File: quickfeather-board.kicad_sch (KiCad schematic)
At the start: 101 parts, among them IC1 EOSAI-S-PUN64, J1 PinHeader_1x2_P2.54mm_Drill1.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, J2 PinHeader_1x12_P2.54m_Drill1.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, J3 61301611121, J4 S2B-PH-SM4-TB(LF)(SN), J5 USB-Micro-B_Molex_473460001, J6 PinHeader_2x5_P1.27mm_SMD_Lat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, J7 PinHeader_1x2_P2.54mm_Drill1.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, J8 PinHeader_2x8_P2.54mm_Drill1mm, M1 mounting_pad, M2 mounting_pad, M3 mounting_pad, M4 mounting_pad, Q1 NX3008CBKV, Q2 2N7002PV, Q3 2N7002PV, Q4 DMG1012T-7, U1 TPS62821DLCR, U2 MCP73831T-2AC_SOT, U3 GD25Q16CWIGR, U4 DPS310, U5 MC3635, X1 Resonator_12MHz_445

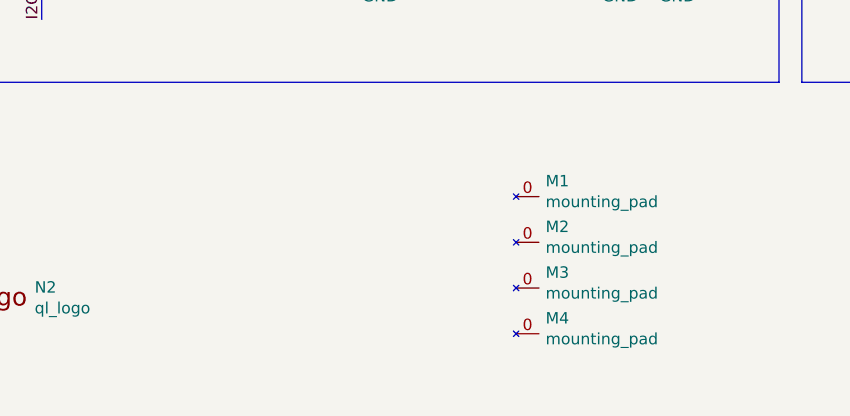
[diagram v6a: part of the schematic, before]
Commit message: [#54927] Add mounting holes
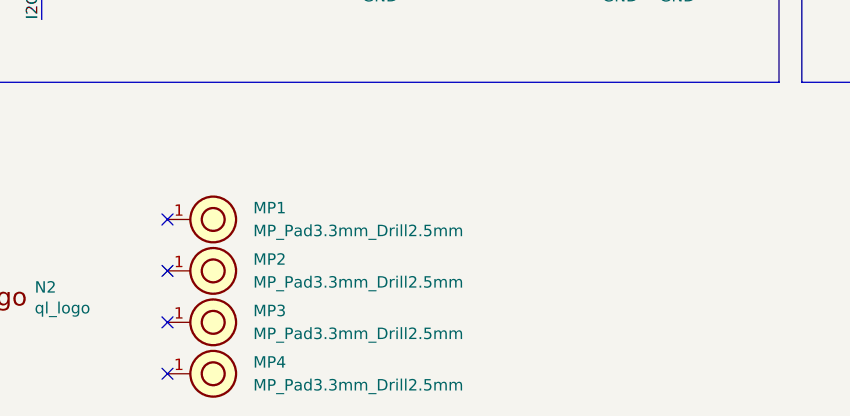
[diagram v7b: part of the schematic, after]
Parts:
- removed M1, M2, M3, M4: mounting_pad, quicklogic-quickfeather-board-footprints:mpad, symbol quickfeather-board:mounting_pad
- added MP1, MP2, MP3, MP4: MP_Pad3.3mm_Drill2.5mm, antmicro-footprints:MP_Pad3.3mm_Drill2.5mm, symbol antmicroMechanicalParts:MP_Pad3.3mm_Drill2.5mm
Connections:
- no-connect marks 23 -> 27
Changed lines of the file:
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@@
   (no_connect (at 344.17 41.91))
   (no_connect (at 389.89 159.385))
+  (no_connect (at 238.125 280.035))
   (no_connect (at 389.255 200.66))
   (no_connect (at 287.02 116.205))
@@
   (no_connect (at 375.92 61.595))
   (no_connect (at 354.33 39.37))
+  (no_connect (at 238.125 268.605))
   (no_connect (at 240.03 95.25))
   (no_connect (at 297.18 116.205))
+  (no_connect (at 238.125 274.32))
   (no_connect (at 27.305 219.075))
   (no_connect (at 297.18 128.905))
   (no_connect (at 359.41 102.87))
+  (no_connect (at 238.125 262.89))
   (no_connect (at 342.9 228.6))
   (no_connect (at 27.305 216.535))
@@
     )
   )
-  (symbol (lib_id "quickfeather-board:mounting_pad") (at 276.86 260.35 0) (unit 1)
-    (in_bom yes) (on_board yes) (dnp no)
-    (property "Reference" "M1" (at 280.1366 258.6228 0)
-      (effects (font (size 1.27 1.27)) (justify left))
-    )
-    (property "Value" "mounting_pad" (at 280.1366 260.9342 0)
-      (effects (font (size 1.27 1.27)) (justify left))
-    )
-    (property "Footprint" "quicklogic-quickfeather-board-footprints:mpad" (at 284.48 263.525 0)
-      (effects (font (size 1.27 1.27)) hide)
-    )
-    (property "Datasheet" "" (at 276.86 260.35 0)
-      (effects (font (size 1.27 1.27)) hide)
-    )
-    (pin "0")
-    (instances
-      (project "quickfeather-board"
-        (path "/902b299f-3bfc-46c5-8ba2-656b16e1e538"
-          (reference "M1") (unit 1)
-        )
-      )
-    )
-  )
-  (symbol (lib_id "quickfeather-board:mounting_pad") (at 276.86 265.43 0) (unit 1)
-    (in_bom yes) (on_board yes) (dnp no)
-    (property "Reference" "M2" (at 280.1366 263.7028 0)
-      (effects (font (size 1.27 1.27)) (justify left))
-    )
-    (property "Value" "mounting_pad" (at 280.1366 266.0142 0)
-      (effects (font (size 1.27 1.27)) (justify left))
-    )
-    (property "Footprint" "quicklogic-quickfeather-board-footprints:mpad" (at 284.48 268.605 0)
-      (effects (font (size 1.27 1.27)) hide)
-    )
-    (property "Datasheet" "" (at 276.86 265.43 0)
-      (effects (font (size 1.27 1.27)) hide)
-    )
-    (pin "0")
-    (instances
-      (project "quickfeather-board"
-        (path "/902b299f-3bfc-46c5-8ba2-656b16e1e538"
-          (reference "M2") (unit 1)
-        )
-      )
-    )
-  )
-  (symbol (lib_id "quickfeather-board:mounting_pad") (at 276.86 270.51 0) (unit 1)
-    (in_bom yes) (on_board yes) (dnp no)
-    (property "Reference" "M3" (at 280.1366 268.7828 0)
-      (effects (font (size 1.27 1.27)) (justify left))
-    )
-    (property "Value" "mounting_pad" (at 280.1366 271.0942 0)
-      (effects (font (size 1.27 1.27)) (justify left))
-    )
-    (property "Footprint" "quicklogic-quickfeather-board-footprints:mpad" (at 284.48 273.685 0)
-      (effects (font (size 1.27 1.27)) hide)
-    )
-    (property "Datasheet" "" (at 276.86 270.51 0)
-      (effects (font (size 1.27 1.27)) hide)
-    )
-    (pin "0")
-    (instances
-      (project "quickfeather-board"
-        (path "/902b299f-3bfc-46c5-8ba2-656b16e1e538"
-          (reference "M3") (unit 1)
-        )
-      )
-    )
-  )
-  (symbol (lib_id "quickfeather-board:mounting_pad") (at 276.86 275.59 0) (unit 1)
-    (in_bom yes) (on_board yes) (dnp no)
-    (property "Reference" "M4" (at 280.1366 273.8628 0)
-      (effects (font (size 1.27 1.27)) (justify left))
-    )
-    (property "Value" "mounting_pad" (at 280.1366 276.1742 0)
-      (effects (font (size 1.27 1.27)) (justify left))
-    )
-    (property "Footprint" "quicklogic-quickfeather-board-footprints:mpad" (at 284.48 278.765 0)
-      (effects (font (size 1.27 1.27)) hide)
-    )
-    (property "Datasheet" "" (at 276.86 275.59 0)
-      (effects (font (size 1.27 1.27)) hide)
-    )
-    (pin "0")
-    (instances
-      (project "quickfeather-board"
-        (path "/902b299f-3bfc-46c5-8ba2-656b16e1e538"
-          (reference "M4") (unit 1)
-        )
-      )
-    )
-  )
   (symbol (lib_id "antmicropower:+3V3") (at 375.285 24.13 0) (unit 1)
     (in_bom yes) (on_board yes) (dnp no)
@@
     )
   )
+  (symbol (lib_id "antmicroMechanicalParts:MP_Pad3.3mm_Drill2.5mm") (at 238.125 280.035 0) (unit 1)
+    (in_bom no) (on_board yes) (dnp no) (fields_autoplaced)
+    (property "Reference" "MP4" (at 247.65 278.765 0)
+      (effects (font (size 1.27 1.27) (thickness 0.15)) (justify left))
+    )
+    (property "Value" "MP_Pad3.3mm_Drill2.5mm" (at 247.65 281.305 0)
+      (effects (font (size 1.27 1.27) (thickness 0.15)) (justify left))
+    )
+    (property "Footprint" "antmicro-footprints:MP_Pad3.3mm_Drill2.5mm" (at 250.825 286.385 0)
+      (effects (font (size 1.27 1.27) (thickness 0.15)) (justify left bottom) hide)
+    )
+    (property "Datasheet" "" (at 254.965 295.605 0)
+      (effects (font (size 1.27 1.27) (thickness 0.15)) (justify left bottom) hide)
+    )
+    (property "License" "Apache-2.0" (at 250.825 291.465 0)
+      (effects (font (size 1.27 1.27)) (justify left bottom) hide)
+    )
+    (property "Author" " Antmicro" (at 249.555 288.925 0)
+      (effects (font (size 1.27 1.27)) (justify left bottom) hide)
+    )
+    (pin "1")
+    (instances
+      (project "quickfeather-board"
+        (path "/902b299f-3bfc-46c5-8ba2-656b16e1e538"
+          (reference "MP4") (unit 1)
+        )
+      )
+    )
+  )
   (symbol (lib_id "antmicropower:+3V3") (at 384.81 24.13 0) (unit 1)
     (in_bom yes) (on_board yes) (dnp no)
@@
     )
   )
+  (symbol (lib_id "antmicroMechanicalParts:MP_Pad3.3mm_Drill2.5mm") (at 238.125 274.32 0) (unit 1)
+    (in_bom no) (on_board yes) (dnp no) (fields_autoplaced)
+    (property "Reference" "MP3" (at 247.65 273.05 0)
+      (effects (font (size 1.27 1.27) (thickness 0.15)) (justify left))
+    )
+    (property "Value" "MP_Pad3.3mm_Drill2.5mm" (at 247.65 275.59 0)
+      (effects (font (size 1.27 1.27) (thickness 0.15)) (justify left))
+    )
+    (property "Footprint" "antmicro-footprints:MP_Pad3.3mm_Drill2.5mm" (at 250.825 280.67 0)
+      (effects (font (size 1.27 1.27) (thickness 0.15)) (justify left bottom) hide)
+    )
+    (property "Datasheet" "" (at 254.965 289.89 0)
+      (effects (font (size 1.27 1.27) (thickness 0.15)) (justify left bottom) hide)
+    )
+    (property "License" "Apache-2.0" (at 250.825 285.75 0)
+      (effects (font (size 1.27 1.27)) (justify left bottom) hide)
+    )
+    (property "Author" " Antmicro" (at 249.555 283.21 0)
+      (effects (font (size 1.27 1.27)) (justify left bottom) hide)
+    )
+    (pin "1")
+    (instances
+      (project "quickfeather-board"
+        (path "/902b299f-3bfc-46c5-8ba2-656b16e1e538"
+          (reference "MP3") (unit 1)
+        )
+      )
+    )
+  )
   (symbol (lib_id "antmicropower:+3V3") (at 366.395 24.13 0) (unit 1)
     (in_bom yes) (on_board yes) (dnp no)
@@
     )
   )
+  (symbol (lib_id "antmicroMechanicalParts:MP_Pad3.3mm_Drill2.5mm") (at 238.125 262.89 0) (unit 1)
+    (in_bom no) (on_board yes) (dnp no) (fields_autoplaced)
+    (property "Reference" "MP1" (at 247.65 261.62 0)
+      (effects (font (size 1.27 1.27) (thickness 0.15)) (justify left))
+    )
+    (property "Value" "MP_Pad3.3mm_Drill2.5mm" (at 247.65 264.16 0)
+      (effects (font (size 1.27 1.27) (thickness 0.15)) (justify left))
+    )
+    (property "Footprint" "antmicro-footprints:MP_Pad3.3mm_Drill2.5mm" (at 250.825 269.24 0)
+      (effects (font (size 1.27 1.27) (thickness 0.15)) (justify left bottom) hide)
+    )
+    (property "Datasheet" "" (at 254.965 278.46 0)
+      (effects (font (size 1.27 1.27) (thickness 0.15)) (justify left bottom) hide)
+    )
+    (property "License" "Apache-2.0" (at 250.825 274.32 0)
+      (effects (font (size 1.27 1.27)) (justify left bottom) hide)
+    )
+    (property "Author" " Antmicro" (at 249.555 271.78 0)
+      (effects (font (size 1.27 1.27)) (justify left bottom) hide)
+    )
+    (pin "1")
+    (instances
+      (project "quickfeather-board"
+        (path "/902b299f-3bfc-46c5-8ba2-656b16e1e538"
+          (reference "MP1") (unit 1)
+        )
+      )
+    )
+  )
   (symbol (lib_id "antmicroCapacitors0603:C_4u7_0603") (at 262.89 177.165 270) (unit 1)
     (in_bom yes) (on_board yes) (dnp no) (fields_autoplaced)
@@
         )
       )
+    )
+  )
+  (symbol (lib_id "antmicroMechanicalParts:MP_Pad3.3mm_Drill2.5mm") (at 238.125 268.605 0) (unit 1)
+    (in_bom no) (on_board yes) (dnp no) (fields_autoplaced)
+    (property "Reference" "MP2" (at 247.65 267.335 0)
+      (effects (font (size 1.27 1.27) (thickness 0.15)) (justify left))
+    )
+    (property "Value" "MP_Pad3.3mm_Drill2.5mm" (at 247.65 269.875 0)
+      (effects (font (size 1.27 1.27) (thickness 0.15)) (justify left))
+    )
+    (property "Footprint" "antmicro-footprints:MP_Pad3.3mm_Drill2.5mm" (at 250.825 274.955 0)
+      (effects (font (size 1.27 1.27) (thickness 0.15)) (justify left bottom) hide)
+    )
+    (property "Datasheet" "" (at 254.965 284.175 0)
+      (effects (font (size 1.27 1.27) (thickness 0.15)) (justify left bottom) hide)
+    )
+    (property "License" "Apache-2.0" (at 250.825 280.035 0)
+      (effects (font (size 1.27 1.27)) (justify left bottom) hide)
+    )
+    (property "Author" " Antmicro" (at 249.555 277.495 0)
+      (effects (font (size 1.27 1.27)) (justify left bottom) hide)
+    )
+    (pin "1")
+    (instances
+      (project "quickfeather-board"
+        (path "/902b299f-3bfc-46c5-8ba2-656b16e1e538"
+          (reference "MP2") (unit 1)
+        )
+      )

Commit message: [#54927] Update X1
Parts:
- X1: value Resonator_12MHz_445 -> Resonator_32.768kHz_ECX-31B; footprint antmicro-footprints:Resonator_SMD_CTS_445_5x3.2mm -> antmicro-footprints:SMD-2_3.2x1.5mm; symbol antmicroResonators:Resonator_12MHz_445 -> antmicroResonators:Resonator_32.768kHz_ECX-31B; MPN 445I23D12M00000 -> ECS-.327-12.5-34B-TR; Manufacturer CTS -> ECS Inc. International; Val 12MHz -> 32.768 kHz
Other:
- moved on the sheet: C6, C7, X1
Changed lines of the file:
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@@
   (junction (at 356.87 130.81) (diameter 0) (color 0 0 0 0)
   )
+  (junction (at 29.21 44.45) (diameter 0) (color 0 0 0 0)
+  )
   (junction (at 396.875 172.085) (diameter 0) (color 0 0 0 0)
   )
@@
   (junction (at 328.93 34.29) (diameter 0) (color 0 0 0 0)
   )
-  (junction (at 31.115 53.34) (diameter 0) (color 0 0 0 0)
-  )
   (junction (at 76.2 124.46) (diameter 0) (color 0 0 0 0)
   )
+  (junction (at 29.21 53.34) (diameter 0) (color 0 0 0 0)
+  )
   (junction (at 15.875 53.34) (diameter 0) (color 0 0 0 0)
   )
@@
   (junction (at 52.705 220.98) (diameter 0) (color 0 0 0 0)
   )
-  (junction (at 31.115 44.45) (diameter 0) (color 0 0 0 0)
-  )
   (junction (at 194.945 158.115) (diameter 0) (color 0 0 0 0)
   )
@@
     (stroke (width 0) (type default))
   )
-  (wire (pts (xy 25.4 53.34) (xy 31.115 53.34))
+  (wire (pts (xy 23.495 53.34) (xy 29.21 53.34))
     (stroke (width 0) (type default))
   )
@@
     (stroke (width 0) (type default))
   )
+  (wire (pts (xy 29.21 53.34) (xy 44.45 53.34))
+    (stroke (width 0) (type default))
+  )
   (wire (pts (xy 178.435 156.21) (xy 178.435 162.56))
     (stroke (width 0) (type default))
@@
     (stroke (width 0) (type default))
   )
-  (wire (pts (xy 15.875 53.34) (xy 20.32 53.34))
+  (wire (pts (xy 15.875 53.34) (xy 18.415 53.34))
     (stroke (width 0) (type default))
   )
@@
     (stroke (width 0) (type default))
   )
-  (wire (pts (xy 15.875 44.45) (xy 20.32 44.45))
+  (wire (pts (xy 15.875 44.45) (xy 18.415 44.45))
     (stroke (width 0) (type default))
   )
@@
     (stroke (width 0) (type default))
   )
-  (wire (pts (xy 31.115 44.45) (xy 44.45 44.45))
+  (wire (pts (xy 29.21 44.45) (xy 44.45 44.45))
     (stroke (width 0) (type default))
   )
@@
     (stroke (width 0) (type default))
   )
-  (wire (pts (xy 25.4 44.45) (xy 31.115 44.45))
+  (wire (pts (xy 23.495 44.45) (xy 29.21 44.45))
     (stroke (width 0) (type default))
   )
@@
     (stroke (width 0) (type default))
   )
-  (wire (pts (xy 31.115 53.34) (xy 31.115 52.705))
+  (wire (pts (xy 29.21 53.34) (xy 29.21 52.705))
     (stroke (width 0) (type default))
   )
@@
     (stroke (width 0) (type default))
   )
-  (wire (pts (xy 31.115 45.085) (xy 31.115 44.45))
+  (wire (pts (xy 29.21 45.085) (xy 29.21 44.45))
     (stroke (width 0) (type default))
   )
@@
     (stroke (width 0) (type default))
   )
-  (wire (pts (xy 44.45 53.34) (xy 31.115 53.34))
-    (stroke (width 0) (type default))
-  )
   (wire (pts (xy 234.315 221.615) (xy 234.315 231.14))
     (stroke (width 0) (type default))
@@
     )
   )
-  (symbol (lib_id "antmicroResonators:Resonator_12MHz_445") (at 31.115 45.085 270) (unit 1)
+  (symbol (lib_id "antmicroResonators:Resonator_32.768kHz_ECX-31B") (at 29.21 45.085 270) (unit 1)
     (in_bom yes) (on_board yes) (dnp no) (fields_autoplaced)
-    (property "Reference" "X1" (at 34.29 47.625 90)
+    (property "Reference" "X1" (at 32.385 47.625 90)
       (effects (font (size 1.27 1.27)) (justify left))
     )
-    (property "Value" "Resonator_12MHz_445" (at 15.875 60.325 0)
+    (property "Value" "Resonator_32.768kHz_ECX-31B" (at 13.97 60.325 0)
       (effects (font (size 1.27 1.27) (thickness 0.15)) (justify left bottom) hide)
     )
-    (property "Footprint" "antmicro-footprints:Resonator_SMD_CTS_445_5x3.2mm" (at 13.335 60.325 0)
+    (property "Footprint" "antmicro-footprints:SMD-2_3.2x1.5mm" (at 11.43 60.325 0)
       (effects (font (size 1.27 1.27) (thickness 0.15)) (justify left bottom) hide)
     )
-    (property "Datasheet" "https://www.ctscorp.com/wp-content/uploads/445.pdf" (at 10.795 60.325 0)
+    (property "Datasheet" "http://www.ecsxtal.com/store/pdf/ecx-31b.pdf" (at 8.89 60.325 0)
       (effects (font (size 1.27 1.27) (thickness 0.15)) (justify left bottom) hide)
     )
-    (property "MPN" "445I23D12M00000" (at 34.925 48.895 90)
-      (effects (font (size 1.27 1.27) (thickness 0.15)) (justify left) hide)
+    (property "MPN" "ECS-.327-12.5-34B-TR" (at 21.59 60.325 0)
+      (effects (font (size 1.27 1.27) (thickness 0.15)) (justify left bottom) hide)
     )
-    (property "Manufacturer" "CTS" (at 20.955 60.325 0)
+    (property "Manufacturer" "ECS Inc. International" (at 19.05 60.325 0)
       (effects (font (size 1.27 1.27) (thickness 0.15)) (justify left bottom) hide)
     )
-    (property "Val" "12MHz" (at 34.29 50.165 90)
+    (property "Val" "32.768 kHz" (at 32.385 50.165 90)
       (effects (font (size 1.27 1.27) (thickness 0.15)) (justify left))
     )
-    (property "Author" "Antmicro" (at 8.255 60.325 0)
+    (property "Author" "Antmicro" (at 6.35 60.325 0)
       (effects (font (size 1.27 1.27) (thickness 0.15)) (justify left bottom) hide)
     )
-    (property "License" "Apache-2.0" (at 5.715 60.325 0)
+    (property "License" "Apache-2.0" (at 3.81 60.325 0)
       (effects (font (size 1.27 1.27) (thickness 0.15)) (justify left bottom) hide)
     )
@@
     )
   )
-  (symbol (lib_id "antmicroCapacitors0402:C_12p_0402") (at 20.32 44.45 0) (unit 1)
+  (symbol (lib_id "antmicroCapacitors0402:C_12p_0402") (at 18.415 44.45 0) (unit 1)
     (in_bom yes) (on_board yes) (dnp no)
-    (property "Reference" "C6" (at 18.415 42.545 0)
+    (property "Reference" "C6" (at 16.51 42.545 0)
       (effects (font (size 1.524 1.524)) (justify left))
     )
-    (property "Value" "C_12p_0402" (at 20.32 48.26 0)
+    (property "Value" "C_12p_0402" (at 18.415 48.26 0)
       (effects (font (size 1.524 1.524)) hide)
     )
-    (property "Footprint" "antmicro-footprints:C_0402_1005Metric" (at 25.4 39.37 0)
+    (property "Footprint" "antmicro-footprints:C_0402_1005Metric" (at 23.495 39.37 0)
       (effects (font (size 1.524 1.524)) (justify left) hide)
     )
-    (property "Datasheet" "https://product.tdk.com/en/search/capacitor/ceramic/mlcc/info?part_no=CGA2B2C0G1H120J050BA" (at 20.32 44.45 0)
+    (property "Datasheet" "https://product.tdk.com/en/search/capacitor/ceramic/mlcc/info?part_no=CGA2B2C0G1H120J050BA" (at 18.415 44.45 0)
       (effects (font (size 1.27 1.27)) hide)
     )
-    (property "Manufacturer" "TDK" (at 25.4 34.29 0)
+    (property "Manufacturer" "TDK" (at 23.495 34.29 0)
       (effects (font (size 1.524 1.524)) (justify left) hide)
     )
-    (property "MPN" "CGA2B2C0G1H120J050BA" (at 25.4 36.83 0)
+    (property "MPN" "CGA2B2C0G1H120J050BA" (at 23.495 36.83 0)
       (effects (font (size 1.524 1.524)) (justify left) hide)
     )
-    (property "Val" "12p" (at 23.495 42.545 0)
+    (property "Val" "12p" (at 21.59 42.545 0)
       (effects (font (size 1.27 1.27)) (justify left))
     )
-    (property "License" "Apache-2.0" (at 40.64 67.31 0)
+    (property "License" "Apache-2.0" (at 38.735 67.31 0)
       (effects (font (size 1.27 1.27) (thickness 0.15)) (justify left bottom) hide)
     )
-    (property "Author" "Antmicro" (at 40.64 69.85 0)
+    (property "Author" "Antmicro" (at 38.735 69.85 0)
       (effects (font (size 1.27 1.27) (thickness 0.15)) (justify left bottom) hide)
     )
-    (property "Voltage" "" (at 40.64 72.39 0)
+    (property "Voltage" "" (at 38.735 72.39 0)
       (effects (font (size 1.27 1.27)) (justify left bottom) hide)
     )
-    (property "Dielectric" "" (at 40.64 74.93 0)
+    (property "Dielectric" "" (at 38.735 74.93 0)
       (effects (font (size 1.27 1.27)) (justify left bottom) hide)
     )
@@
     )
   )
-  (symbol (lib_id "antmicroCapacitors0402:C_12p_0402") (at 25.4 53.34 180) (unit 1)
+  (symbol (lib_id "antmicroCapacitors0402:C_12p_0402") (at 23.495 53.34 180) (unit 1)
     (in_bom yes) (on_board yes) (dnp no)
-    (property "Reference" "C7" (at 20.32 51.435 0)
+    (property "Reference" "C7" (at 18.415 51.435 0)
       (effects (font (size 1.524 1.524)))
     )
-    (property "Value" "C_12p_0402" (at 25.4 49.53 0)
+    (property "Value" "C_12p_0402" (at 23.495 49.53 0)
       (effects (font (size 1.524 1.524)) hide)
     )
-    (property "Footprint" "antmicro-footprints:C_0402_1005Metric" (at 20.32 58.42 0)
+    (property "Footprint" "antmicro-footprints:C_0402_1005Metric" (at 18.415 58.42 0)
       (effects (font (size 1.524 1.524)) (justify left) hide)
     )
-    (property "Datasheet" "https://product.tdk.com/en/search/capacitor/ceramic/mlcc/info?part_no=CGA2B2C0G1H120J050BA" (at 25.4 53.34 0)
+    (property "Datasheet" "https://product.tdk.com/en/search/capacitor/ceramic/mlcc/info?part_no=CGA2B2C0G1H120J050BA" (at 23.495 53.34 0)
       (effects (font (size 1.27 1.27)) hide)
     )
-    (property "Manufacturer" "TDK" (at 20.32 63.5 0)
+    (property "Manufacturer" "TDK" (at 18.415 63.5 0)
       (effects (font (size 1.524 1.524)) (justify left) hide)
     )
-    (property "MPN" "CGA2B2C0G1H120J050BA" (at 20.32 60.96 0)
+    (property "MPN" "CGA2B2C0G1H120J050BA" (at 18.415 60.96 0)
       (effects (font (size 1.524 1.524)) (justify left) hide)
     )
-    (property "Val" "12p" (at 26.035 51.435 0)
+    (property "Val" "12p" (at 24.13 51.435 0)
       (effects (font (size 1.27 1.27)))
     )
-    (property "License" "Apache-2.0" (at 5.08 30.48 0)
+    (property "License" "Apache-2.0" (at 3.175 30.48 0)
       (effects (font (size 1.27 1.27) (thickness 0.15)) (justify left bottom) hide)
     )
-    (property "Author" "Antmicro" (at 5.08 27.94 0)
+    (property "Author" "Antmicro" (at 3.175 27.94 0)
       (effects (font (size 1.27 1.27) (thickness 0.15)) (justify left bottom) hide)
     )
-    (property "Voltage" "" (at 5.08 25.4 0)
+    (property "Voltage" "" (at 3.175 25.4 0)
       (effects (font (size 1.27 1.27)) (justify left bottom) hide)
     )
-    (property "Dielectric" "" (at 5.08 22.86 0)
+    (property "Dielectric" "" (at 3.175 22.86 0)
       (effects (font (size 1.27 1.27)) (justify left bottom) hide)
     )
